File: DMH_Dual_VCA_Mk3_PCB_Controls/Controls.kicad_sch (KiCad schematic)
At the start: 27 parts, among them SW1 SW_DPDT_3way, U9 TL074

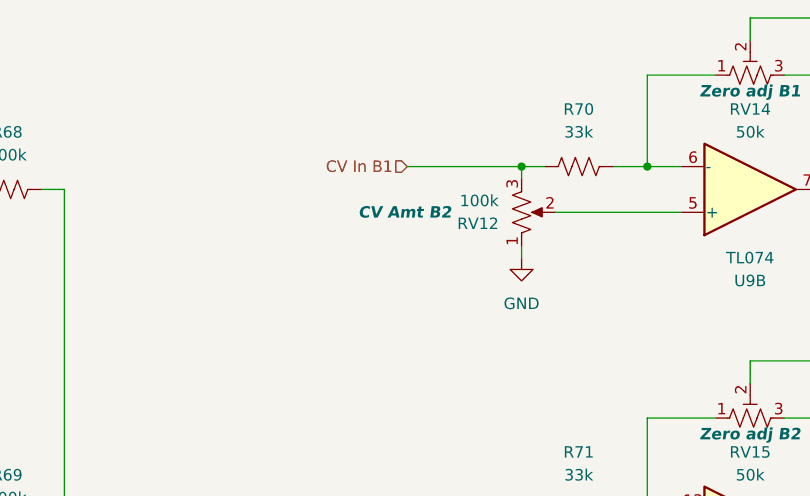
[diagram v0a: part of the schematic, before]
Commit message: Controls PCB comp placement started
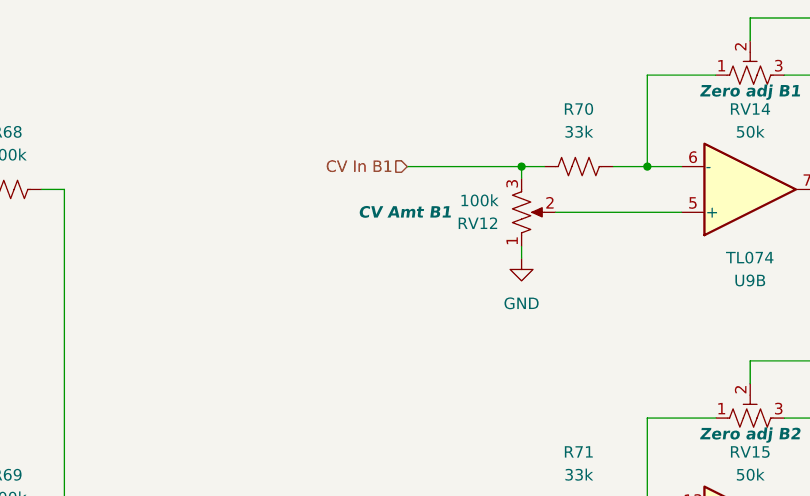
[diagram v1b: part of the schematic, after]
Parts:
- RV12: Function CV Amt B2 -> CV Amt B1
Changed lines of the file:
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@@
 			)
 		)
-		(property "Function" "CV Amt B2"
+		(property "Function" "CV Amt B1"
 			(at 126.746 40.64 0)
 			(show_name no)

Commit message: Moved clipping circuit back to main PCB
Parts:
- RV10, RV14, RV15, RV9: footprint Potentiometer_THT:Potentiometer_Bourns_3296W_Vertical -> Potentiometer_THT:Potentiometer_Bourns_3296X_Horizontal
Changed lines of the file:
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@@
 			)
 		)
-		(property "Footprint" "Potentiometer_THT:Potentiometer_Bourns_3296W_Vertical"
+		(property "Footprint" "Potentiometer_THT:Potentiometer_Bourns_3296X_Horizontal"
 			(at 165.1 25.4 0)
 			(hide yes)
@@
 			)
 		)
-		(property "Footprint" "Potentiometer_THT:Potentiometer_Bourns_3296W_Vertical"
+		(property "Footprint" "Potentiometer_THT:Potentiometer_Bourns_3296X_Horizontal"
 			(at 63.5 25.4 0)
 			(hide yes)
@@
 			)
 		)
-		(property "Footprint" "Potentiometer_THT:Potentiometer_Bourns_3296W_Vertical"
+		(property "Footprint" "Potentiometer_THT:Potentiometer_Bourns_3296X_Horizontal"
 			(at 165.1 63.5 0)
 			(hide yes)
@@
 			)
 		)
-		(property "Footprint" "Potentiometer_THT:Potentiometer_Bourns_3296W_Vertical"
+		(property "Footprint" "Potentiometer_THT:Potentiometer_Bourns_3296X_Horizontal"
 			(at 63.5 63.5 0)
 			(hide yes)

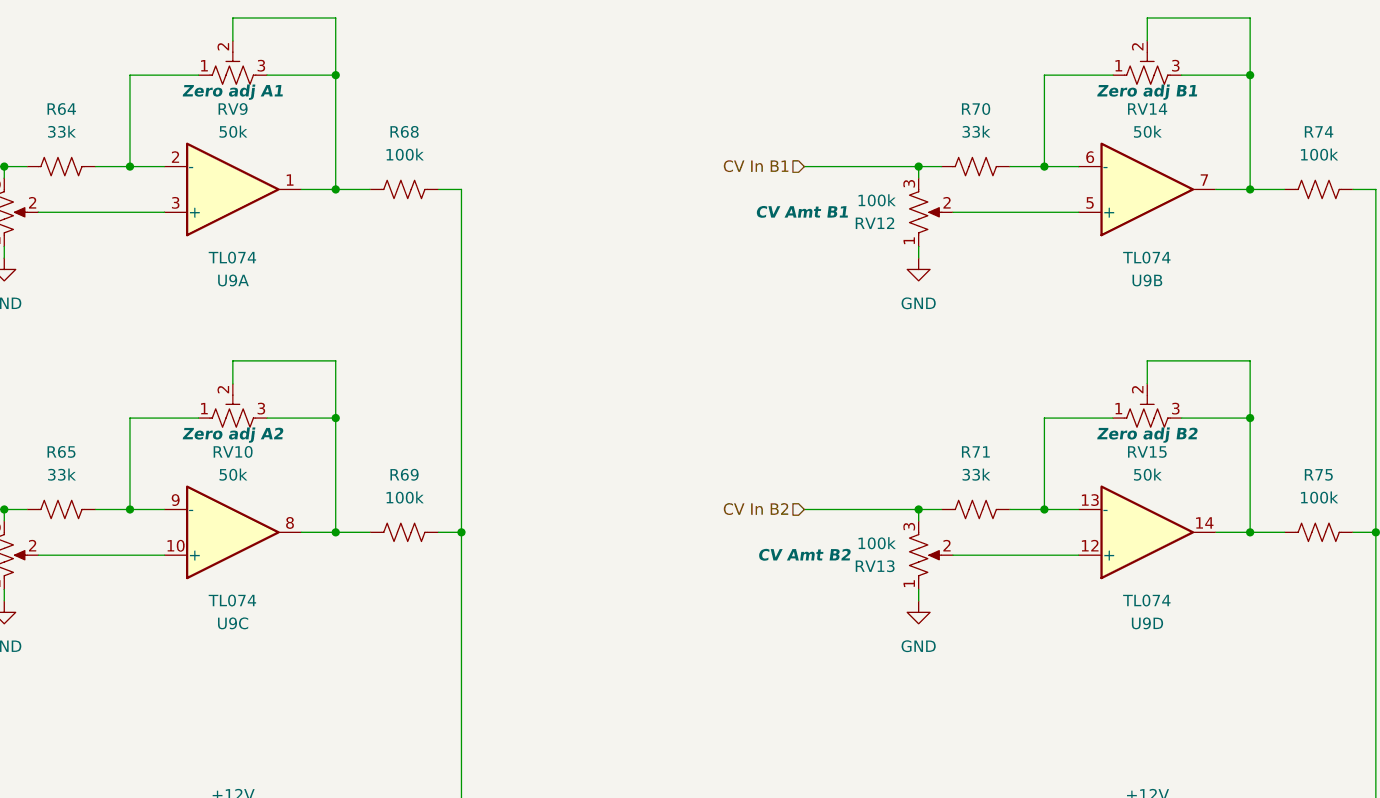
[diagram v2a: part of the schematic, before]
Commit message: Controls PCB comp placement in progress
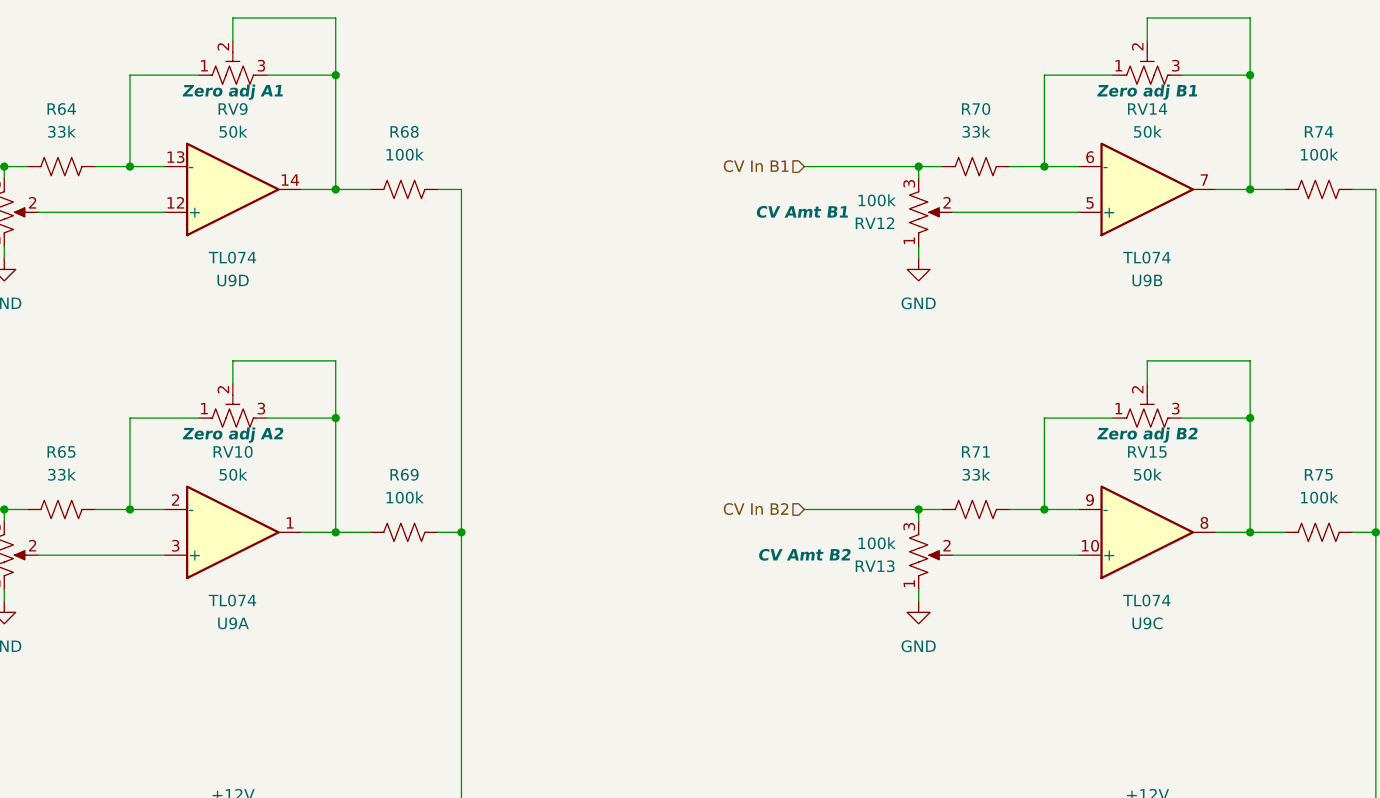
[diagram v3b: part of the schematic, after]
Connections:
- net at R71.2, RV15.1: now also U9.9 (-); no longer U9.13 (-)
- net at RV8.2: now also U9.3 (+); no longer U9.10 (+)
- net at R69.1, RV10.2, RV10.3: now also U9.1; no longer U9.8
- net at R65.2, RV10.1: now also U9.2 (-); no longer U9.9 (-)
- net at RV13.2: now also U9.10 (+); no longer U9.12 (+)
- net at R75.1, RV15.2, RV15.3: now also U9.8; no longer U9.14
- net at R68.1, RV9.2, RV9.3: now also U9.14; no longer U9.1
- net at R64.2, RV9.1: now also U9.13 (-); no longer U9.2 (-)
- net at RV7.2: now also U9.12 (+); no longer U9.3 (+)
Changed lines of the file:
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@@
 		(at 63.5 76.2 0)
 		(mirror x)
-		(unit 3)
+		(unit 1)
 		(body_style 1)
 		(exclude_from_sim no)
@@
 				(path "/58f4306d-5387-4983-bb08-41a2313fd315/aca37be5-e58c-41bf-b28c-79389d66daa4"
 					(reference "U9")
-					(unit 3)
+					(unit 1)
 				)
 			)
@@
 		(at 165.1 76.2 0)
 		(mirror x)
-		(unit 4)
+		(unit 3)
 		(body_style 1)
 		(exclude_from_sim no)
@@
 				(path "/58f4306d-5387-4983-bb08-41a2313fd315/aca37be5-e58c-41bf-b28c-79389d66daa4"
 					(reference "U9")
-					(unit 4)
+					(unit 3)
 				)
 			)
@@
 		(at 63.5 38.1 0)
 		(mirror x)
-		(unit 1)
+		(unit 4)
 		(body_style 1)
 		(exclude_from_sim no)
@@
 				(path "/58f4306d-5387-4983-bb08-41a2313fd315/aca37be5-e58c-41bf-b28c-79389d66daa4"
 					(reference "U9")
-					(unit 1)
-				)
-			)
+					(unit 4)
+				)
+			)
